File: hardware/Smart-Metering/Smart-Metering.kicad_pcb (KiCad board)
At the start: 4 copper layers, 130 x 130 mm, 227 parts, among them J101 AUX L N, J201 VA VB VC VN, J301 SENSOR_IA, J302 SENSOR_IB, J303 SENSOR_IC, J304 SENSOR_IN, J501 SWD, J701 HMI_LINK, J801 RS485, J802 USB-C, J901 BATTERY_1S, SW901 POWER, U401 ADE9430ACPZ, U501 STM32F413RHT6, U502 24LC64, U601 ISO7762DW, U602 ISO7761DW, U604 MCP3204, U605 TPS7A2033PDBVR, U606 ADuM6000, U801 ADM2587E, U802 USBLC6-2SC6, U901 BQ25895RTW, U902 TPS63001, U903 TPS61022, Y401 24.576MHz, Y501 8MHz, Y502 32.768kHz

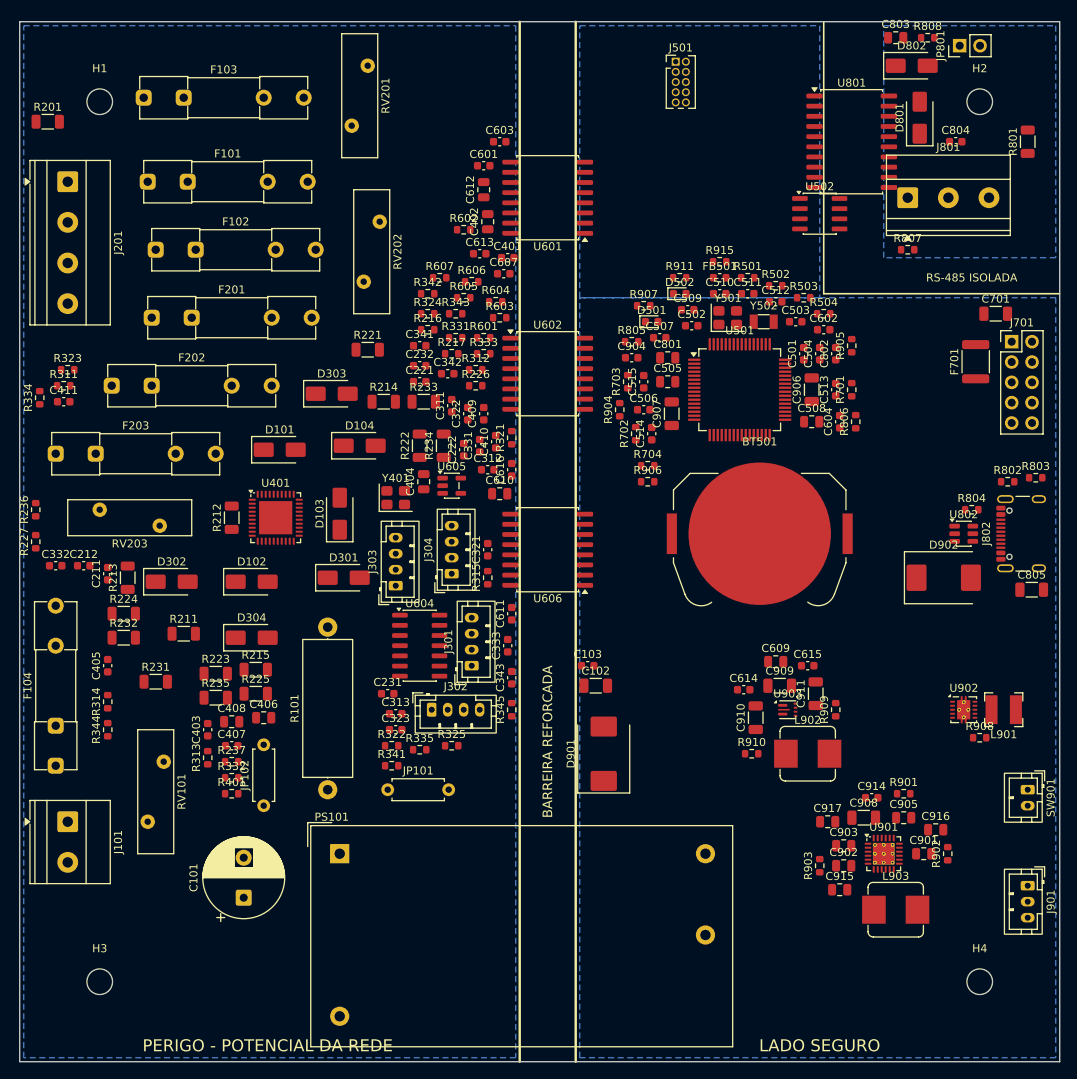
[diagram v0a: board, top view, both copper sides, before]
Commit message: Reorganiza o posicionamento do domínio quente para o roteamento
- barreira principal movida para x = 75-82 mm: o lado da rede e da
  metrologia ganha 12,5 mm; isoladores e ADuM6000 acompanham;
- entradas de tensão em linhas por fase (borne -> fusível -> varistor
  -> cadeia do divisor em linha reta), espaçadas para 3 mm entre fases;
- entradas de corrente em linhas por canal (conector -> TVS -> Ra/Rb ->
  filtro), ao lado do ADE9430;
- desacoplamentos, cristal e filtros posicionados junto ao pino exato
  do CI a que se ligam;
- peças de rede restritas à faixa superior e ao canto inferior esquerdo
  (nunca no núcleo metrológico);
- classes: HVBUS para o barramento HV; MAINS com clearance base de
  0,5 mm e 3 mm só entre redes diferentes; creepage entre fases em
  3 mm; exceções para pads internos de bornes e retificadores de rede.

Checkpoint antes do roteamento (ainda sem trilhas).

Co-Authored-By: Claude Opus 5.5 <noreply@anthropic.com>
Claude-Session: https://claude.ai/code/session_012B8cVkhtjf3eg98UdpNCpf
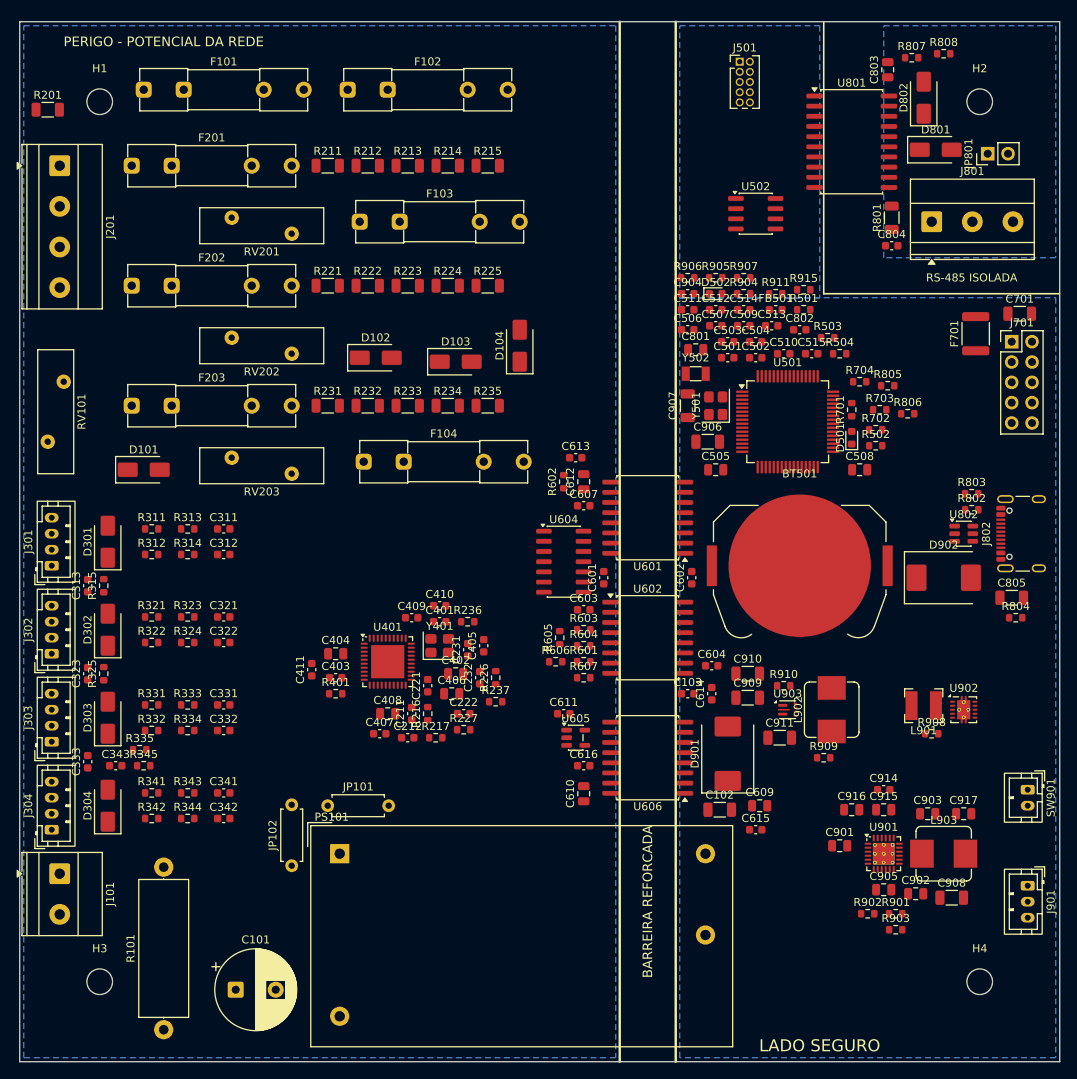
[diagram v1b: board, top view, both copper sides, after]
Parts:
- moved R342 74.1 mm to (56.5, 129.6)
- moved R215 69.4 mm to (98.5, 48.0)
- moved R343 68.6 mm to (61.0, 126.4)
- moved R213 62.3 mm to (88.5, 48.0), turned to 0 degrees
- moved C342 62.3 mm to (65.5, 129.6)
- moved R211 61.2 mm to (78.5, 48.0)
- moved C341 61.0 mm to (65.5, 126.4)
- moved R331 59.6 mm to (56.5, 115.4)
- moved C603 59.4 mm to (110.5, 103.5)
- moved J304 59.4 mm to (44.0, 131.0)
- moved R225 58.7 mm to (98.5, 63.0)
- moved R227 58.4 mm to (95.5, 118.5), turned to 0 degrees
- moved R224 57.6 mm to (93.5, 63.0)
- moved R333 57.4 mm to (61.0, 115.4)
- moved C402 56.6 mm to (94.5, 111.5), turned to 0 degrees
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
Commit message: Ajusta posicionamento e regras para o roteamento do domínio quente
- R201 (ligação neutro -> GND) junto do pino de neutro do J201;
- peças de rede automáticas não invadem a linha da fase C;
- footprints: pads só de pasta/máscara deixam de ser tratados como cobre;
- regra "Entrada dos retificadores de rede" (2,4 mm para trilhas que
  chegam aos D101-D104, cujo encapsulamento SMA tem ~2 mm entre
  terminais).

Checkpoint antes do roteamento (ainda sem trilhas).

Co-Authored-By: Claude Opus 5.5 <noreply@anthropic.com>
Claude-Session: https://claude.ai/code/session_012B8cVkhtjf3eg98UdpNCpf
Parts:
- moved D102 67.2 mm to (67.5, 137.0), turned to 90 degrees
- moved RV101 64.8 mm to (108.0, 76.5)
- moved R201 28.5 mm to (49.0, 69.0), turned to 90 degrees
- moved D103 19.9 mm to (110.0, 60.0)
- moved D104 18.6 mm to (110.0, 53.5), turned to 0 degrees
- moved F104 14.5 mm to (82.5, 70.5)
- moved R909 13.5 mm to (133.5, 110.5)
- moved D101 11.0 mm to (47.5, 78.5), turned to 90 degrees
- moved C910 8.86 mm to (139.5, 114.0), turned to 90 degrees
- moved C911 6.73 mm to (130.0, 115.0)
- moved L902 6.26 mm to (138.5, 121.5), turned to 0 degrees
- moved C613 4.47 mm to (107.5, 88.5)
- moved C909 4.27 mm to (135.0, 113.0)
- moved R602 3.64 mm to (107.0, 91.0), turned to 0 degrees
- moved R910 3.35 mm to (137.0, 110.0)
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
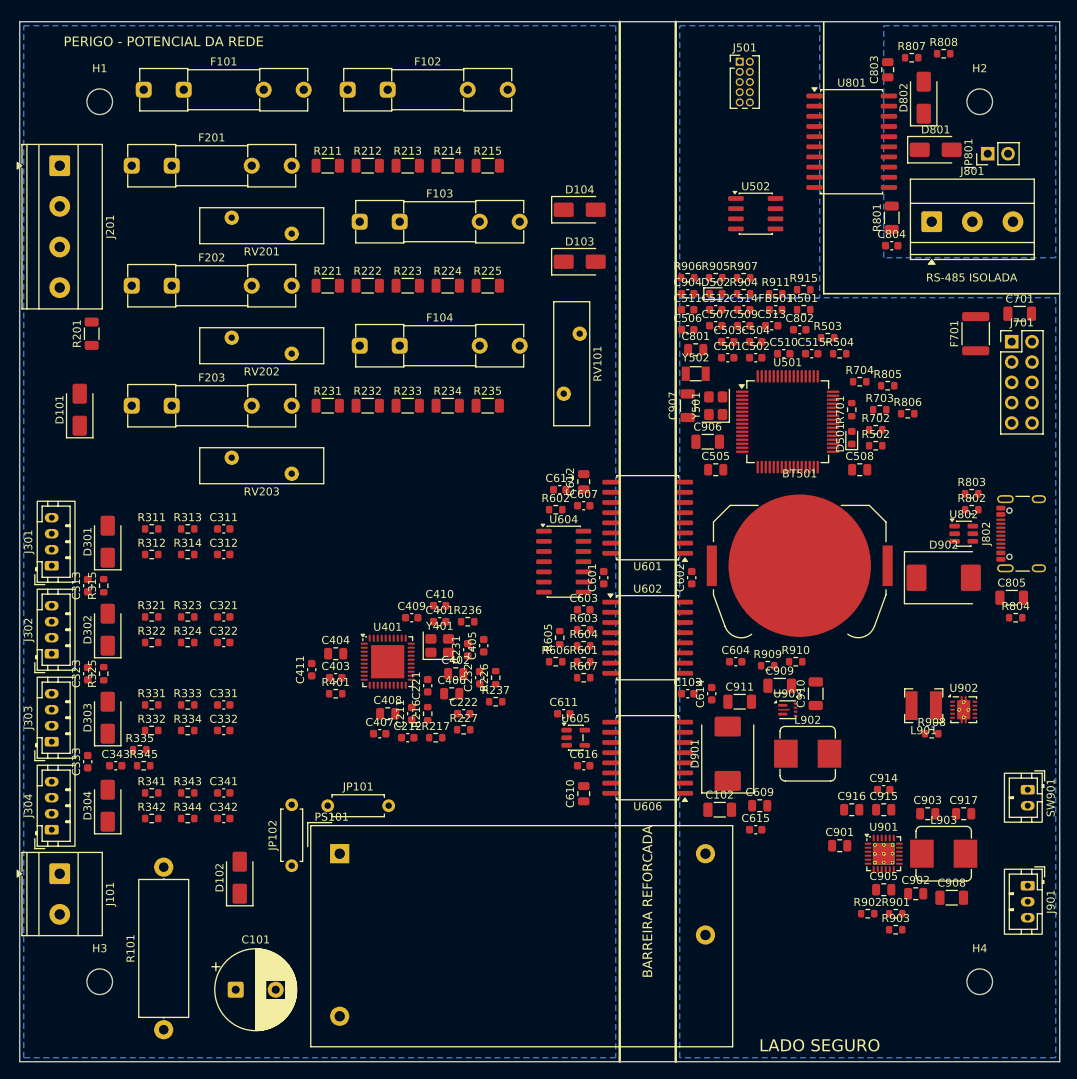
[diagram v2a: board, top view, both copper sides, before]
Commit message: Reposiciona retificadores D101-D104 junto dos fusíveis e alinha U401 à grade
D101-D104 agrupados ao lado de F101-F104 (catodo comum voltado para a
barreira), evitando que as nets de fase cruzem as linhas das outras fases.
U401 deslocado 0,05 mm para que os pads de passo 0,5 mm caiam na grade de
roteamento de 0,1 mm.

Co-Authored-By: Claude Opus 5.5 <noreply@anthropic.com>
Claude-Session: https://claude.ai/code/session_012B8cVkhtjf3eg98UdpNCpf
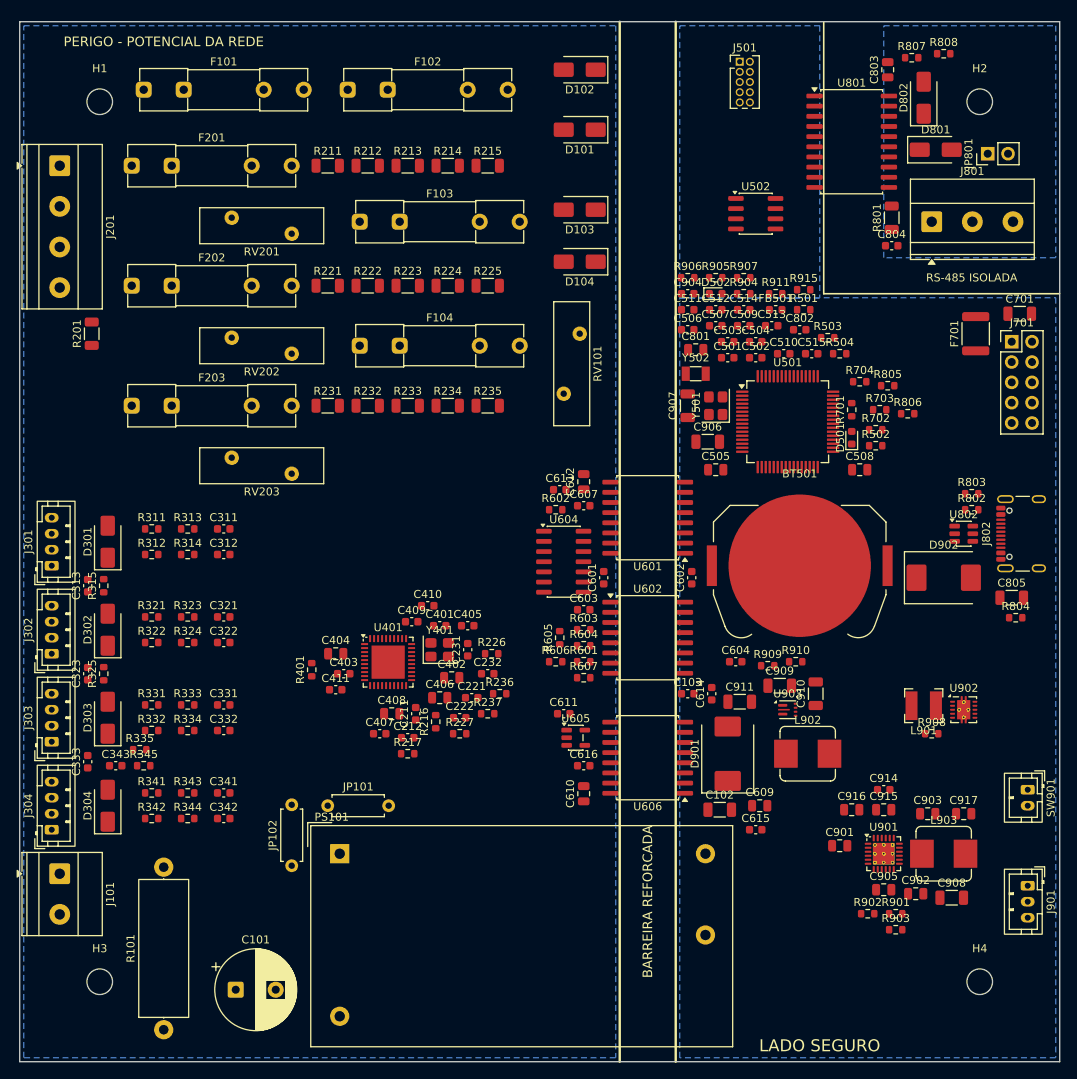
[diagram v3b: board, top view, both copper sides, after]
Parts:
- moved D102 109.6 mm to (110.0, 36.0), turned to 180 degrees
- moved D101 71.6 mm to (110.0, 43.5), turned to 180 degrees
- moved R236 9.85 mm to (100.0, 114.0)
- moved D103 6.50 mm to (110.0, 53.5), turned to 180 degrees
- moved D104 6.50 mm to (110.0, 60.0), turned to 180 degrees
- moved C221 5.70 mm to (96.5, 114.5), turned to 0 degrees
- moved R401 4.24 mm to (76.5, 111.0), turned to 90 degrees
- moved R217 4.03 mm to (88.5, 121.5)
- moved C411 3.91 mm to (79.5, 113.5), turned to 0 degrees
- moved C405 3.20 mm to (96.0, 105.5), turned to 0 degrees
- moved R226 3.04 mm to (99.0, 109.0), turned to 0 degrees
- moved R237 1.80 mm to (98.5, 116.5)
- moved C406 1.58 mm to (92.5, 114.5)
- moved C410 1.50 mm to (91.0, 103.0)
- moved R216 1.41 mm to (92.0, 117.5)
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
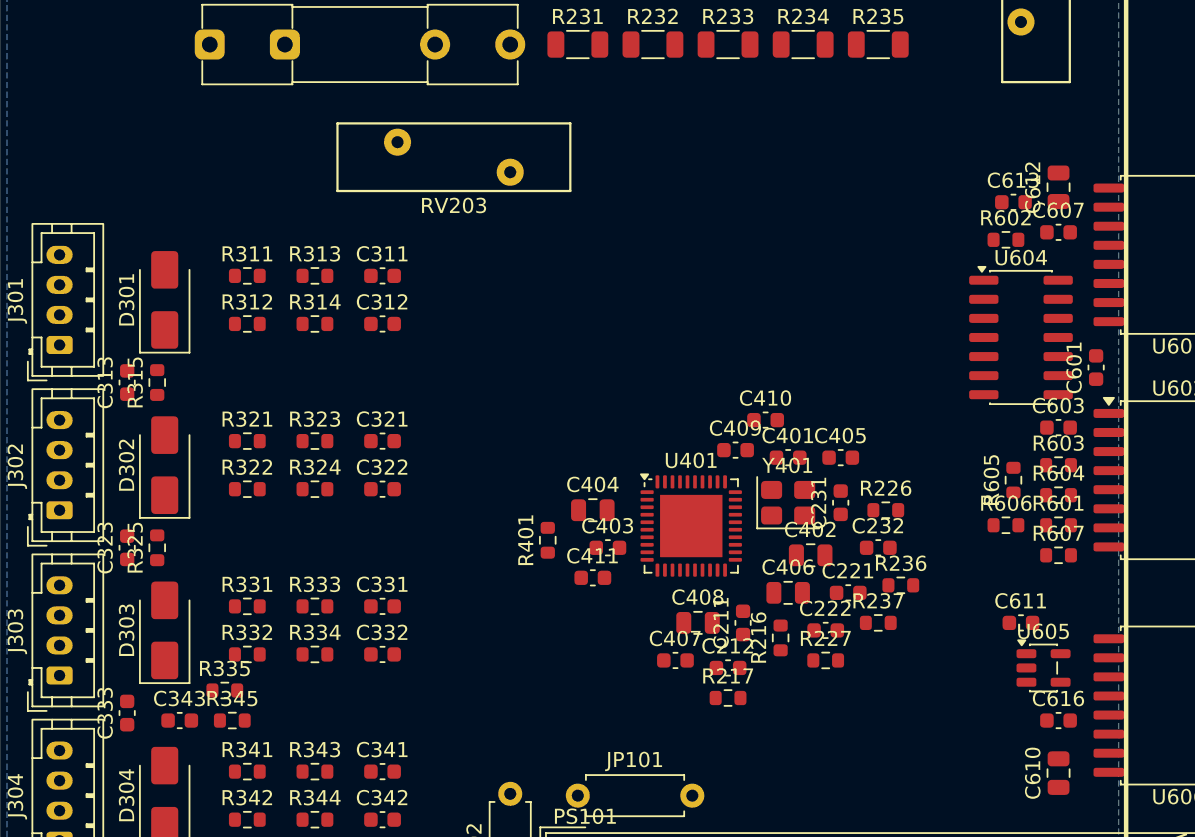
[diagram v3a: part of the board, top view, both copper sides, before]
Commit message: Reorganiza o entorno do ADE9430 para o roteamento
- conjunto do ADE9430 deslocado 4 mm para a esquerda, abrindo uma coluna
  (x ~ 61 mm) para o barramento retificado D101-D104 -> R101/PS101
  passar sem atravessar os filtros das entradas de tensão;
- U604 (MCP3204) ao lado do ADE, do mesmo lado do barramento;
- C403/C404 (DVDDOUT) junto dos pinos 1-3 e RC do RESET acima do CI,
  liberando o lado esquerdo para as entradas de corrente (pinos 7-14);
- C401/C405 e C409/C410 fora da saída dos pinos digitais (31-40).

Co-Authored-By: Claude Opus 5.5 <noreply@anthropic.com>
Claude-Session: https://claude.ai/code/session_012B8cVkhtjf3eg98UdpNCpf
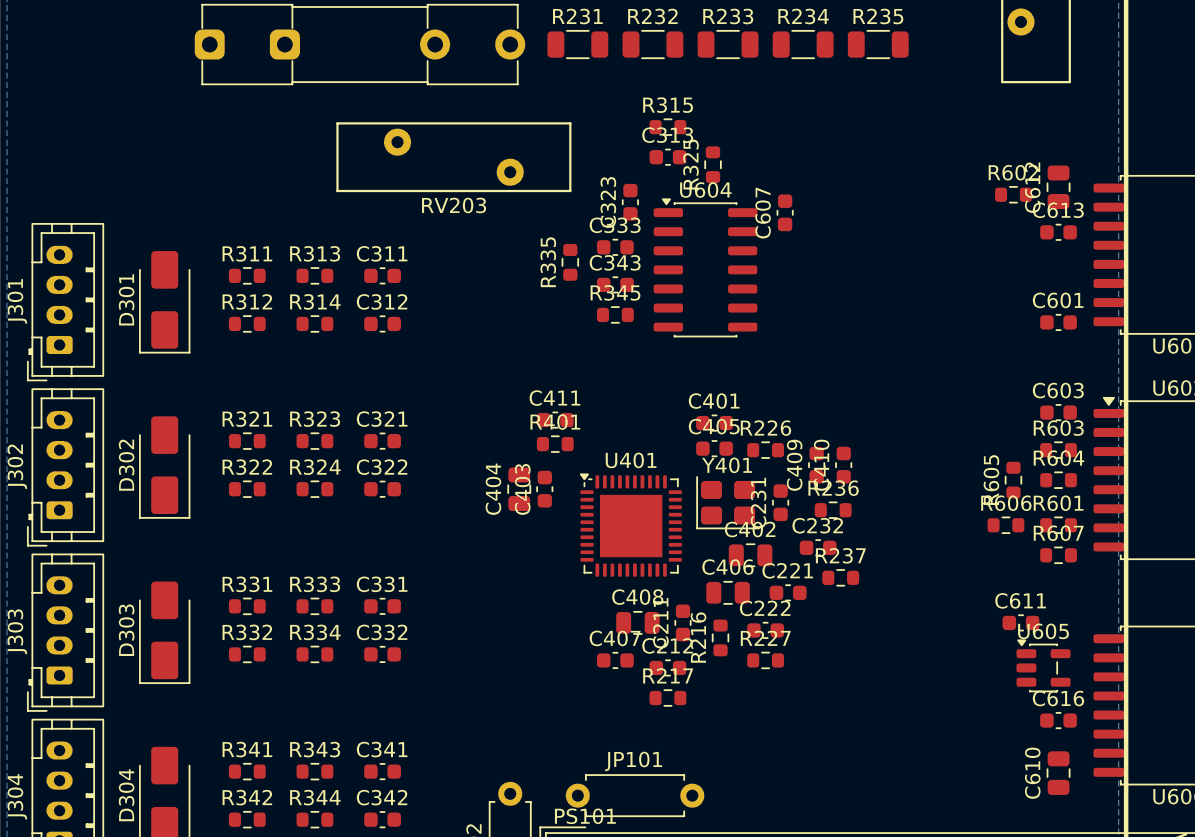
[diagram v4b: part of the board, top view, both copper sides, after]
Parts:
- moved R325 44.9 mm to (87.5, 86.0)
- moved C333 44.9 mm to (81.0, 91.5), turned to 0 degrees
- moved C343 41.0 mm to (81.0, 94.0)
- moved C323 40.6 mm to (82.0, 88.5)
- moved C313 39.0 mm to (84.5, 85.5), turned to 0 degrees
- moved R315 38.0 mm to (84.5, 83.5), turned to 0 degrees
- moved R345 37.1 mm to (81.0, 96.0)
- moved R335 36.6 mm to (78.0, 92.5), turned to 90 degrees
- moved U604 21.5 mm to (87.0, 93.0)
- moved C607 18.2 mm to (92.3, 89.2), turned to 90 degrees
- moved C411 10.8 mm to (77.0, 103.0)
- moved R226 8.94 mm to (91.0, 105.0)
- moved C405 8.42 mm to (87.6, 104.9)
- moved R236 6.73 mm to (95.5, 109.0)
- moved R401 6.42 mm to (77.0, 104.6), turned to 0 degrees
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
